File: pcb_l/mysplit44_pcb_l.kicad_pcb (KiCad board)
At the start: 2 copper layers, 133.3 x 104.8 mm, 47 parts, among them J1 MJ-4PP-9, SW1 SW_PUSH, SW10 SW_PUSH, SW11 SW_PUSH, SW12 SW_PUSH, SW13 SW_PUSH, SW14 SW_PUSH, SW15 SW_PUSH, SW16 SW_PUSH, SW17 SW_PUSH, SW18 SW_PUSH, SW19 SW_PUSH, SW2 SW_PUSH, SW20 SW_PUSH, SW21 SW_PUSH, SW22 SW_PUSH, SW3 SW_PUSH, SW4 SW_PUSH, SW5 SW_PUSH, SW6 SW_PUSH, SW7 SW_PUSH, SW8 SW_PUSH, SW9 SW_PUSH, U1 ProMicro

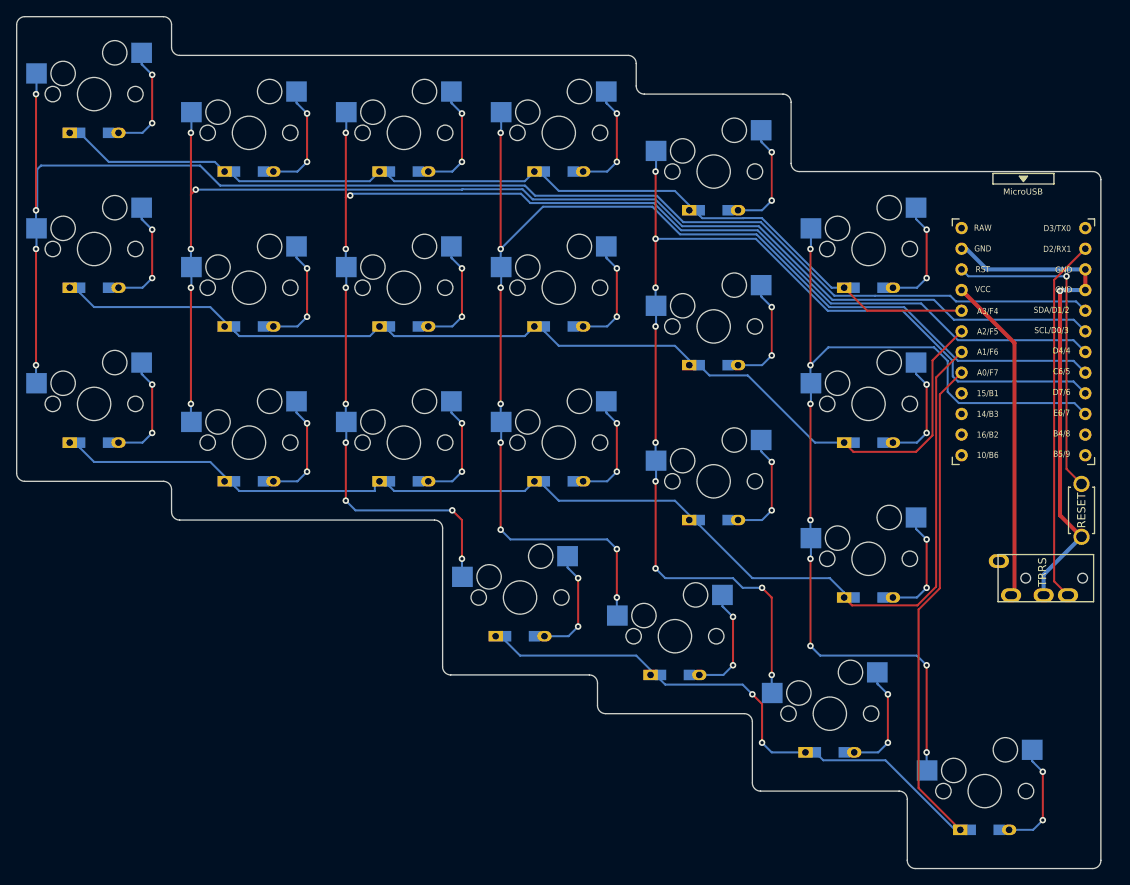
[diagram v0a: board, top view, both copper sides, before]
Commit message: added topplate-l, fixed pcb-l hole
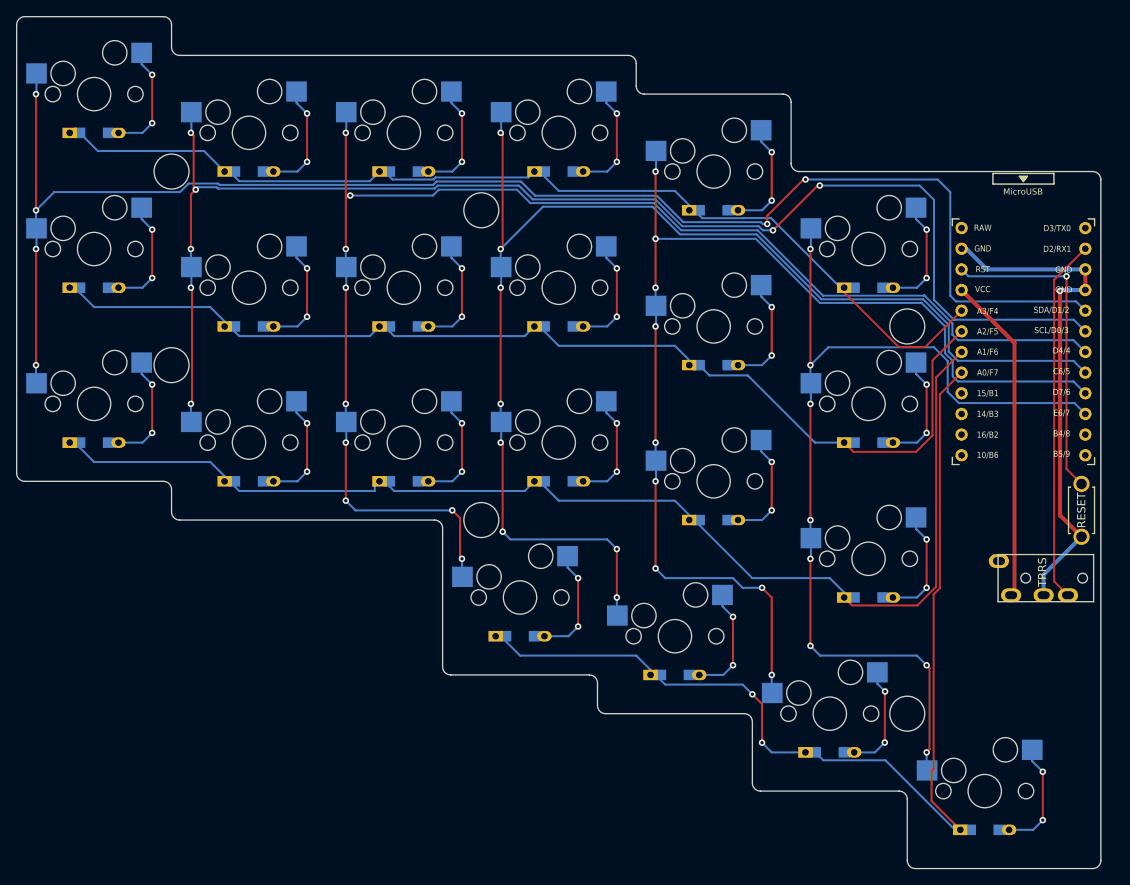
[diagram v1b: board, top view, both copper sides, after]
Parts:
- added Ref**: Val**, kbd:spacer_m2, F.Cu at (38.1, 40.5)
- added Ref**: Val**, kbd:spacer_m2, F.Cu at (76.2, 83.3)
- added Ref**: Val**, kbd:spacer_m2, F.Cu at (38.1, 64.3)
- added Ref**: Val**, kbd:spacer_m2, F.Cu at (128.6, 59.5)
- added Ref**: Val**, kbd:spacer_m2, F.Cu at (128.6, 107.2)
- added Ref**: Val**, kbd:spacer_m2, F.Cu at (76.2, 45.2)
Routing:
- net COL2: track 155.9 -> 167.7 mm, vias 5 -> 7
- net COL1: track 179.8 -> 188.1 mm, vias 4 -> 6
- net ROW1: track 116.4 -> 120.2 mm
- net COL4: track 157.5 -> 159.6 mm
- net COL5: track 140.9 -> 142.8 mm
- net ROW4: track 127.8 -> 126.4 mm
- net COL3: track 169.4 -> 170.7 mm
- net Net-(D21-A): track 13.8 -> 13.3 mm

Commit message: added gnd mask
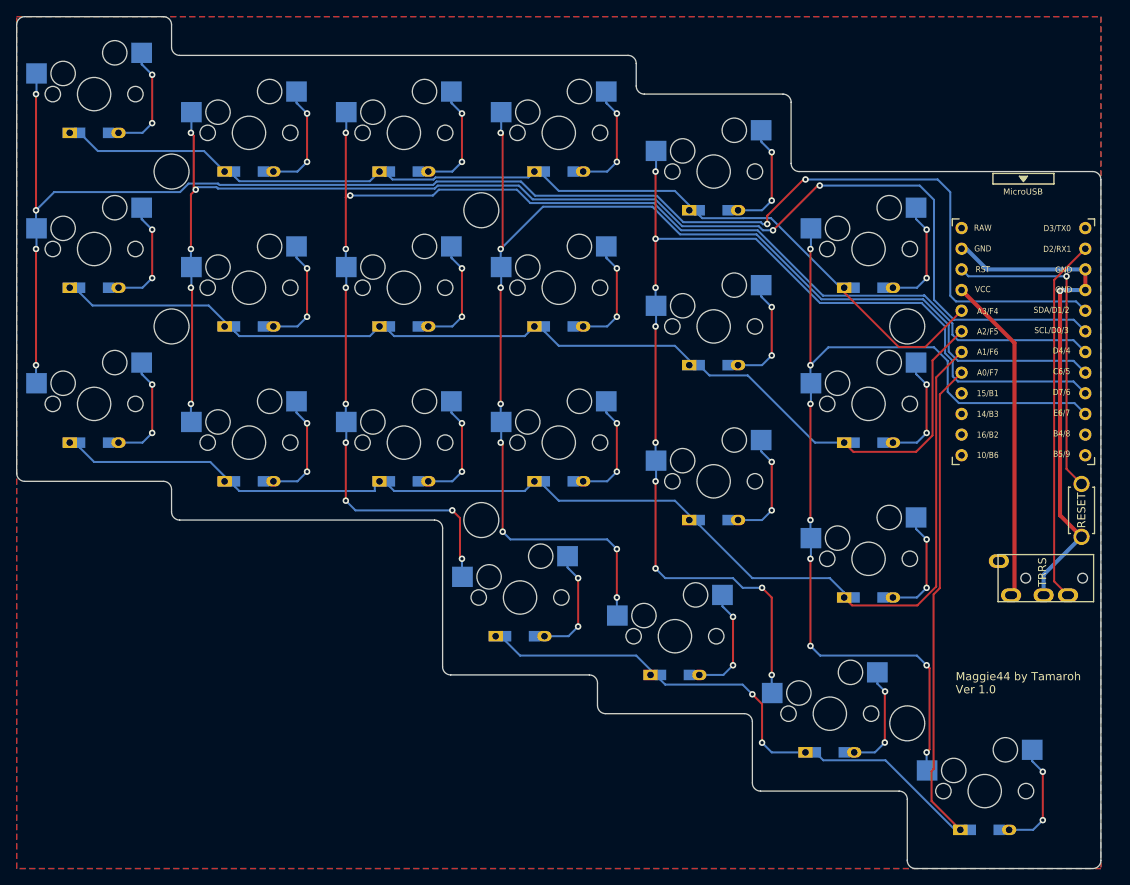
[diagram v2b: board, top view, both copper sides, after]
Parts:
- moved Ref** 4.76 mm to (38.1, 59.5)
- moved Ref** 1.19 mm to (128.6, 108.3)
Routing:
- added copper zone on B.Cu, net GND
- added copper zone on F.Cu, net GND
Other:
- board text added: "Maggie44 by Tamaroh Ver 1.0"
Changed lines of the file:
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@@
   )
   (footprint "kbd:spacer_m2" (layer "F.Cu")
-    (at 38.1 64.29375)
+    (at 38.1 59.53125)
     (descr "Mounting Hole 2.2mm, no annular, M2")
     (tags "mounting hole 2.2mm no annular m2")
@@
   )
   (footprint "kbd:spacer_m2" (layer "F.Cu")
-    (at 128.5875 107.15625)
+    (at 128.5875 108.346875)
     (descr "Mounting Hole 2.2mm, no annular, M2")
     (tags "mounting hole 2.2mm no annular m2")
@@
   (gr_line (start 152.4 125.20625) (end 152.4 41.48125)
     (stroke (width 0.1) (type default)) (layer "Edge.Cuts"))
+  (gr_text "Maggie44 by Tamaroh\nVer 1.0" (at 134.540625 104.775) (layer "F.SilkS")
+    (effects (font (size 1 1) (thickness 0.15)) (justify left bottom))
+  )
   (segment (start 135.2664 57.5945) (end 130.80465 62.05625) (width 0.25) (layer "F.Cu") (net 1))
   (segment (start 127.541611 62.05625) (end 120.825 55.339639) (width 0.25) (layer "F.Cu") (net 1))
@@
   (segment (start 135.2664 60.1345) (end 131.69375 63.70715) (width 0.25) (layer "F.Cu") (net 8))
   (segment (start 131.69375 72.92843) (end 129.66593 74.95625) (width 0.25) (layer "F.Cu") (net 8))
+  (segment (start 28.38125 56.95625) (end 42.66875 56.95625) (width 0.25) (layer "B.Cu") (net 8))
   (segment (start 83.95 59.53125) (end 83.95 60.1375) (width 0.25) (layer "B.Cu") (net 8))
   (segment (start 64.9 60.1375) (end 65.484375 60.721875) (width 0.25) (layer "B.Cu") (net 8))
@@
   (segment (start 108.975 65.55625) (end 117.2375 73.81875) (width 0.25) (layer "B.Cu") (net 8))
   (segment (start 104.2625 65.55625) (end 108.975 65.55625) (width 0.25) (layer "B.Cu") (net 8))
+  (segment (start 26.8 55.375) (end 28.38125 56.95625) (width 0.25) (layer "B.Cu") (net 8))
   (segment (start 26.8 54.76875) (end 26.8 55.375) (width 0.25) (layer "B.Cu") (net 8))
-  (segment (start 42.8625 57.15) (end 44.625 58.9125) (width 0.25) (layer "B.Cu") (net 8))
   (segment (start 46.434375 60.721875) (end 62.484375 60.721875) (width 0.25) (layer "B.Cu") (net 8))
+  (segment (start 44.625 58.9125) (end 44.625 59.53125) (width 0.25) (layer "B.Cu") (net 8))
   (segment (start 81.534375 60.721875) (end 82.725 59.53125) (width 0.25) (layer "B.Cu") (net 8))
-  (segment (start 26.8 55.375) (end 28.575 57.15) (width 0.25) (layer "B.Cu") (net 8))
   (segment (start 117.2375 73.81875) (end 120.825 73.81875) (width 0.25) (layer "B.Cu") (net 8))
   (segment (start 101.775 63.675) (end 101.775 64.29375) (width 0.25) (layer "B.Cu") (net 8))
   (segment (start 103 64.29375) (end 104.2625 65.55625) (width 0.25) (layer "B.Cu") (net 8))
-  (segment (start 28.575 57.15) (end 42.8625 57.15) (width 0.25) (layer "B.Cu") (net 8))
   (segment (start 100.0125 61.9125) (end 101.775 63.675) (width 0.25) (layer "B.Cu") (net 8))
   (segment (start 64.9 59.53125) (end 64.9 60.1375) (width 0.25) (layer "B.Cu") (net 8))
   (segment (start 85.725 61.9125) (end 100.0125 61.9125) (width 0.25) (layer "B.Cu") (net 8))
-  (segment (start 44.625 58.9125) (end 44.625 59.53125) (width 0.25) (layer "B.Cu") (net 8))
   (segment (start 83.95 60.1375) (end 85.725 61.9125) (width 0.25) (layer "B.Cu") (net 8))
   (segment (start 45.85 59.53125) (end 45.85 60.1375) (width 0.25) (layer "B.Cu") (net 8))
+  (segment (start 42.66875 56.95625) (end 44.625 58.9125) (width 0.25) (layer "B.Cu") (net 8))
   (segment (start 62.484375 60.721875) (end 63.675 59.53125) (width 0.25) (layer "B.Cu") (net 8))
   (segment (start 35.71875 47.625) (end 35.71875 53.578125) (width 0.25) (layer "F.Cu") (net 9))
@@
   (segment (start 149.14815 68.95625) (end 134.930899 68.95625) (width 0.25) (layer "B.Cu") (net 37))
   (segment (start 117.871875 100.0125) (end 129.778125 100.0125) (width 0.25) (layer "B.Cu") (net 37))
+  (zone (net 28) (net_name "GND") (layers "F&B.Cu") (hatch edge 0.5)
+    (connect_pads (clearance 0.5))
+    (min_thickness 0.25) (filled_areas_thickness no)
+    (fill yes (thermal_gap 0.5) (thermal_bridge_width 0.5))
+    (polygon
+      (pts
+        (xy 19.05 21.43125)
+        (xy 152.4 21.43125)
+        (xy 152.4 126.20625)
+        (xy 19.05 126.20625)
+      )
+    )
+  )
   (group "" (id b9ec9487-7741-4b36-bab2-a6f5571cd5b5)
     (members
